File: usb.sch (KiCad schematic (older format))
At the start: 10 parts, among them J1 USB_B_Micro, Q1 2N2219, Q2 2N2219, U2 CP2102N-A01-GQFN28, U6 USBLC6-2SC6

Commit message: Reorganize symbols & update vendors
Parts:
- Q2: renamed from Q1; value 2N2219 -> ?
- Q3: renamed from Q2; value 2N2219 -> ?
- R4: renamed from R1; value 22.1 Ohm -> 22k Ohm; Vendor (none) -> avt.pl; VendorLink (none) -> https://sklep.avt.pl/avt701-805.html
- R5: renamed from R2; value 47.5 Ohm -> 47k Ohm; Vendor (none) -> avt.pl; VendorLink (none) -> https://sklep.avt.pl/avt701-805.html
- R6: renamed from R4; value 2k Ohm -> 2.2k Ohm; Vendor (none) -> avt.pl; VendorLink (none) -> https://sklep.avt.pl/avt701-805.html
- R7: renamed from R6; Vendor (none) -> avt.pl; VendorLink (none) -> https://sklep.avt.pl/avt701-805.html
- R8: renamed from R7; Vendor (none) -> avt.pl; VendorLink (none) -> https://sklep.avt.pl/avt701-805.html
- renumbered J1 to J6, U6 to U5, U2 to U6
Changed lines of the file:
@@
 P 5350 3700
 AR Path="/5FFBA0ED" Ref="U?"  Part="1"
-AR Path="/5FF73D59/5FFBA0ED" Ref="U2"  Part="1"
-F 0 "U2" H 5350 2300 50  0000 C CNN
-F 1 "CP2102N-A01-GQFN28" H 5350 2200 50  0000 C CNN
+AR Path="/5FF73D59/5FFBA0ED" Ref="U6"  Part="1"
+F 0 "U6" H 4900 4950 50  0000 C CNN
+F 1 "CP2102N-A01-GQFN28" H 5900 2350 50  0000 C CNN
 F 2 "Package_DFN_QFN:QFN-28-1EP_5x5mm_P0.5mm_EP3.35x3.35mm" H 5800 2500 50  0001 L CNN
 F 3 "https://www.silabs.com/documents/public/data-sheets/cp2102n-datasheet.pdf" H 5400 2950 50  0001 C CNN
@@
 P 5350 5350
 AR Path="/5FFBA0F3" Ref="#PWR?"  Part="1"
-AR Path="/5FF73D59/5FFBA0F3" Ref="#PWR05"  Part="1"
-F 0 "#PWR05" H 5350 5100 50  0001 C CNN
+AR Path="/5FF73D59/5FFBA0F3" Ref="#PWR027"  Part="1"
+F 0 "#PWR027" H 5350 5100 50  0001 C CNN
 F 1 "GND" H 5400 5150 50  0000 C CNN
 F 2 "" H 5350 5350 50  0001 C CNN
@@
 P 4750 2550
 AR Path="/5FFBA107" Ref="R?"  Part="1"
-AR Path="/5FF73D59/5FFBA107" Ref="R4"  Part="1"
-F 0 "R4" H 4900 2500 50  0000 R CNN
-F 1 "2k Ohm" H 5100 2600 50  0000 R CNN
+AR Path="/5FF73D59/5FFBA107" Ref="R6"  Part="1"
+F 0 "R6" H 4900 2500 50  0000 R CNN
+F 1 "2.2k Ohm" H 5100 2600 50  0000 R CNN
 F 2 "Resistor_SMD:R_0805_2012Metric_Pad1.20x1.40mm_HandSolder" V 4680 2550 50  0001 C CNN
 F 3 "~" H 4750 2550 50  0001 C CNN
+F 4 "avt.pl" H 4750 2550 50  0001 C CNN "Vendor"
+F 5 "https://sklep.avt.pl/avt701-805.html" H 4750 2550 50  0001 C CNN "VendorLink"
 	1    4750 2550
 	-1   0    0    1
@@
 P 4150 3300
 AR Path="/5FFBA115" Ref="R?"  Part="1"
-AR Path="/5FF73D59/5FFBA115" Ref="R2"  Part="1"
-F 0 "R2" H 4350 3250 50  0000 R CNN
-F 1 "47.5 Ohm" H 4600 3350 50  0000 R CNN
+AR Path="/5FF73D59/5FFBA115" Ref="R5"  Part="1"
+F 0 "R5" H 4350 3250 50  0000 R CNN
+F 1 "47k Ohm" H 4600 3350 50  0000 R CNN
 F 2 "Resistor_SMD:R_0805_2012Metric_Pad1.20x1.40mm_HandSolder" V 4080 3300 50  0001 C CNN
 F 3 "~" H 4150 3300 50  0001 C CNN
+F 4 "avt.pl" H 4150 3300 50  0001 C CNN "Vendor"
+F 5 "https://sklep.avt.pl/avt701-805.html" H 4150 3300 50  0001 C CNN "VendorLink"
 	1    4150 3300
 	-1   0    0    1
@@
 P 4150 2750
 AR Path="/5FFBA123" Ref="R?"  Part="1"
-AR Path="/5FF73D59/5FFBA123" Ref="R1"  Part="1"
-F 0 "R1" H 4300 2700 50  0000 R CNN
-F 1 "22.1 Ohm" H 4600 2800 50  0000 R CNN
+AR Path="/5FF73D59/5FFBA123" Ref="R4"  Part="1"
+F 0 "R4" H 4300 2700 50  0000 R CNN
+F 1 "22k Ohm" H 4600 2800 50  0000 R CNN
 F 2 "Resistor_SMD:R_0805_2012Metric_Pad1.20x1.40mm_HandSolder" V 4080 2750 50  0001 C CNN
 F 3 "~" H 4150 2750 50  0001 C CNN
+F 4 "avt.pl" H 4150 2750 50  0001 C CNN "Vendor"
+F 5 "https://sklep.avt.pl/avt701-805.html" H 4150 2750 50  0001 C CNN "VendorLink"
 	1    4150 2750
 	-1   0    0    1
@@
 P 4150 3650
 AR Path="/5FFBA14D" Ref="#PWR?"  Part="1"
-AR Path="/5FF73D59/5FFBA14D" Ref="#PWR03"  Part="1"
-F 0 "#PWR03" H 4150 3400 50  0001 C CNN
+AR Path="/5FF73D59/5FFBA14D" Ref="#PWR026"  Part="1"
+F 0 "#PWR026" H 4150 3400 50  0001 C CNN
 F 1 "GND" H 4200 3450 50  0000 C CNN
 F 2 "" H 4150 3650 50  0001 C CNN
@@
 P 1550 2650
 AR Path="/5FFC9948" Ref="J?"  Part="1"
-AR Path="/5FF73D59/5FFC9948" Ref="J1"  Part="1"
-F 0 "J1" H 1650 3150 50  0000 C CNN
+AR Path="/5FF73D59/5FFC9948" Ref="J6"  Part="1"
+F 0 "J6" H 1650 3150 50  0000 C CNN
 F 1 "USB_B_Micro" H 1650 3050 50  0000 C CNN
 F 2 "Connector_USB:USB_Micro-B_Molex_47346-0001" H 1700 2600 50  0001 C CNN
@@
 P 8600 2700
 AR Path="/5FFD7260" Ref="Q?"  Part="1"
-AR Path="/5FF73D59/5FFD7260" Ref="Q1"  Part="1"
-F 0 "Q1" H 8800 2750 50  0000 L CNN
-F 1 "2N2219" H 8800 2700 50  0000 L CNN
+AR Path="/5FF73D59/5FFD7260" Ref="Q2"  Part="1"
+F 0 "Q2" H 8800 2750 50  0000 L CNN
+F 1 "?" H 8800 2700 50  0000 L CNN
 F 2 "Package_TO_SOT_SMD:SOT-23" H 8800 2625 50  0001 L CIN
 F 3 "https://www.onsemi.com/pub/Collateral/BC808-D.pdf" H 8600 2700 50  0001 L CNN
@@
 P 8600 3250
 AR Path="/5FFD7266" Ref="Q?"  Part="1"
-AR Path="/5FF73D59/5FFD7266" Ref="Q2"  Part="1"
-F 0 "Q2" H 8850 3300 50  0000 L CNN
-F 1 "2N2219" H 8850 3250 50  0000 L CNN
+AR Path="/5FF73D59/5FFD7266" Ref="Q3"  Part="1"
+F 0 "Q3" H 8850 3300 50  0000 L CNN
+F 1 "?" H 8850 3250 50  0000 L CNN
 F 2 "Package_TO_SOT_SMD:SOT-23" H 8800 3175 50  0001 L CIN
 F 3 "https://www.onsemi.com/pub/Collateral/BC808-D.pdf" H 8600 3250 50  0001 L CNN
@@
 P 8100 2700
 AR Path="/5FFD726C" Ref="R?"  Part="1"
-AR Path="/5FF73D59/5FFD726C" Ref="R6"  Part="1"
-F 0 "R6" V 7850 2700 50  0000 C CNN
+AR Path="/5FF73D59/5FFD726C" Ref="R7"  Part="1"
+F 0 "R7" V 7850 2700 50  0000 C CNN
 F 1 "10k Ohm" V 7950 2700 50  0000 C CNN
 F 2 "Resistor_SMD:R_0805_2012Metric_Pad1.20x1.40mm_HandSolder" V 8030 2700 50  0001 C CNN
 F 3 "~" H 8100 2700 50  0001 C CNN
+F 4 "avt.pl" H 8100 2700 50  0001 C CNN "Vendor"
+F 5 "https://sklep.avt.pl/avt701-805.html" H 8100 2700 50  0001 C CNN "VendorLink"
 	1    8100 2700
 	0    1    1    0
@@
 P 8100 3250
 AR Path="/5FFD7272" Ref="R?"  Part="1"
-AR Path="/5FF73D59/5FFD7272" Ref="R7"  Part="1"
-F 0 "R7" V 7850 3250 50  0000 C CNN
+AR Path="/5FF73D59/5FFD7272" Ref="R8"  Part="1"
+F 0 "R8" V 7850 3250 50  0000 C CNN
 F 1 "10k Ohm" V 7950 3250 50  0000 C CNN
 F 2 "Resistor_SMD:R_0805_2012Metric_Pad1.20x1.40mm_HandSolder" V 8030 3250 50  0001 C CNN
 F 3 "~" H 8100 3250 50  0001 C CNN
+F 4 "avt.pl" H 8100 3250 50  0001 C CNN "Vendor"
+F 5 "https://sklep.avt.pl/avt701-805.html" H 8100 3250 50  0001 C CNN "VendorLink"
 	1    8100 3250
 	0    1    1    0
@@
 P 1800 4000
 AR Path="/5FFC9960" Ref="#PWR?"  Part="1"
-AR Path="/5FF73D59/5FFC9960" Ref="#PWR02"  Part="1"
-F 0 "#PWR02" H 1800 3750 50  0001 C CNN
+AR Path="/5FF73D59/5FFC9960" Ref="#PWR025"  Part="1"
+F 0 "#PWR025" H 1800 3750 50  0001 C CNN
 F 1 "GND" H 1850 3800 50  0000 C CNN
 F 2 "" H 1800 4000 50  0001 C CNN
@@
 Connection ~ 1800 3850
 $Comp
-L Power_Protection:USBLC6-2SC6 U6
+L Power_Protection:USBLC6-2SC6 U5
 U 1 1 601988F8
 P 2450 3200
-F 0 "U6" H 2450 3800 50  0000 C CNN
-F 1 "USBLC6-2SC6" H 2450 3700 50  0000 C CNN
+F 0 "U5" H 2700 3550 50  0000 C CNN
+F 1 "USBLC6-2SC6" H 2150 2800 50  0000 C CNN
 F 2 "Package_TO_SOT_SMD:SOT-23-6" H 2450 2700 50  0001 C CNN
 F 3 "https://www.st.com/resource/en/datasheet/usblc6-2.pdf" H 2650 3550 50  0001 C CNN

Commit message: Remove Op-Amp circuit for USB power
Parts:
- added D?: STPS0520Z, Diode_SMD:D_0805_2012Metric_Pad1.15x1.40mm_HandSolder, symbol Device:D_Schottky
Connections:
- net VBUS: now also D?.2 (A)
- new net +5V: D?.1 (K)
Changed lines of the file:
@@
 Wire Wire Line
 	4150 2200 3900 2200
-Text HLabel 3050 2450 2    50   Output ~ 0
-VBUS
 Text Label 2850 2450 2    50   ~ 0
 VBUS
@@
 Connection ~ 2450 2450
 Wire Wire Line
-	2450 2450 3050 2450
+	2450 2450 2850 2450
 Wire Wire Line
 	1550 3850 1800 3850
@@
 Wire Wire Line
 	5350 1850 5350 2300
+$Comp
+L Device:D_Schottky D?
+U 1 1 5FB2216A
+P 3000 5850
+AR Path="/5FB2216A" Ref="D?"  Part="1"
+AR Path="/5FF6344B/5FB2216A" Ref="D?"  Part="1"
+F 0 "D?" H 3000 5600 50  0000 C CNN
+F 1 "STPS0520Z" H 3000 5700 50  0000 C CNN
+F 2 "Diode_SMD:D_0805_2012Metric_Pad1.15x1.40mm_HandSolder" H 3000 5850 50  0001 C CNN
+F 3 "https://www.st.com/resource/en/datasheet/stps0520z.pdf" H 3000 5850 50  0001 C CNN
+F 4 "tme.eu" H 3000 5850 50  0001 C CNN "Vendor"
+F 5 "https://www.tme.eu/pl/details/stps0520z/diody-schottky-smd/stmicroelectronics/" H 3000 5850 50  0001 C CNN "VendorLink"
+	1    3000 5850
+	-1   0    0    1
+$EndComp
+Wire Wire Line
+	3150 5850 3650 5850
+Wire Wire Line
+	2200 5850 2850 5850
+Text HLabel 3650 5850 2    50   UnSpc ~ 0
++5V
+Text Label 2200 5850 0    50   ~ 0
+VBUS
 $EndSCHEMATC

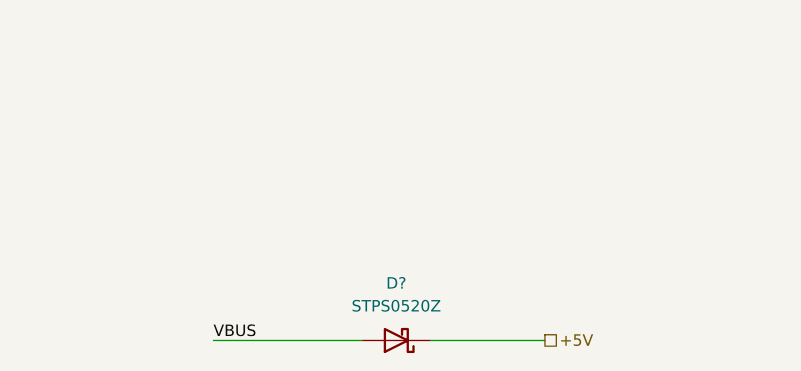
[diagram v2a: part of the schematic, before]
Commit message: Change footprint of D3
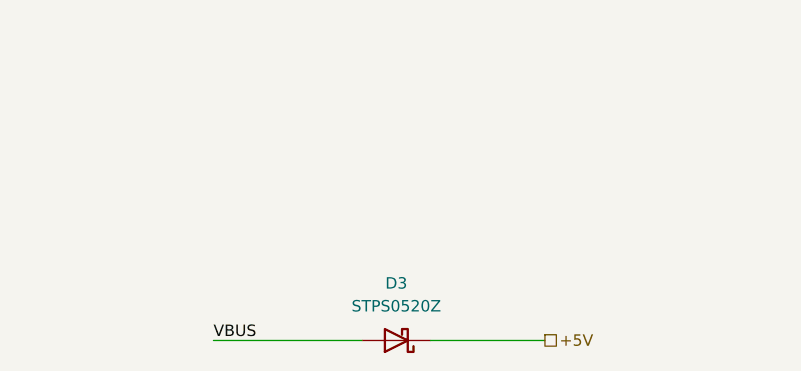
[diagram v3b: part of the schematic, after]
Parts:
- D3: renamed from D?; footprint Diode_SMD:D_0805_2012Metric_Pad1.15x1.40mm_HandSolder -> Diode_SMD:D_SOD-123
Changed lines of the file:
@@
 AR Path="/5FB2216A" Ref="D?"  Part="1"
 AR Path="/5FF6344B/5FB2216A" Ref="D?"  Part="1"
-F 0 "D?" H 3000 5600 50  0000 C CNN
+AR Path="/5FF73D59/5FB2216A" Ref="D3"  Part="1"
+F 0 "D3" H 3000 5600 50  0000 C CNN
 F 1 "STPS0520Z" H 3000 5700 50  0000 C CNN
-F 2 "Diode_SMD:D_0805_2012Metric_Pad1.15x1.40mm_HandSolder" H 3000 5850 50  0001 C CNN
+F 2 "Diode_SMD:D_SOD-123" H 3000 5850 50  0001 C CNN
 F 3 "https://www.st.com/resource/en/datasheet/stps0520z.pdf" H 3000 5850 50  0001 C CNN
 F 4 "tme.eu" H 3000 5850 50  0001 C CNN "Vendor"

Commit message: Update vendor for USB-UART and USBLC6
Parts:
- U5: Vendor (none) -> tme.eu; VendorLink (none) -> https://www.tme.eu/pl/details/usblc6-2sc6/diody-zabezpiecza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
- U6: Vendor (none) -> tme.eu; VendorLink (none) -> https://www.tme.eu/pl/details/cp2102-gm/uklady-scalone-inte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
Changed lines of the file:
@@
 F 2 "Package_DFN_QFN:QFN-28-1EP_5x5mm_P0.5mm_EP3.35x3.35mm" H 5800 2500 50  0001 L CNN
 F 3 "https://www.silabs.com/documents/public/data-sheets/cp2102n-datasheet.pdf" H 5400 2950 50  0001 C CNN
+F 4 "tme.eu" H 5350 3700 50  0001 C CNN "Vendor"
+F 5 "https://www.tme.eu/pl/details/cp2102-gm/uklady-scalone-interfejs-usb/silicon-labs/cp2102-gmr/" H 5350 3700 50  0001 C CNN "VendorLink"
 	1    5350 3700
 	1    0    0    -1
@@
 F 2 "Package_TO_SOT_SMD:SOT-23-6" H 2450 2700 50  0001 C CNN
 F 3 "https://www.st.com/resource/en/datasheet/usblc6-2.pdf" H 2650 3550 50  0001 C CNN
+F 4 "tme.eu" H 2450 3200 50  0001 C CNN "Vendor"
+F 5 "https://www.tme.eu/pl/details/usblc6-2sc6/diody-zabezpieczajace-drabinki/stmicroelectronics/" H 2450 3200 50  0001 C CNN "VendorLink"
 	1    2450 3200
 	-1   0    0    -1

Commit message: Fix auto-reset circuit for ESP32
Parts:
- Q2, Q3: symbol Transistor_BJT:BC807 -> Transistor_BJT:BC817
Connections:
- net DTR: now also Q3.2 (E); no longer Q3.3 (C)
- net IO0: now also Q3.3 (C); no longer Q3.2 (E)
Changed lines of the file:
@@
 RTS
 $Comp
-L Transistor_BJT:BC807 Q?
+L Transistor_BJT:BC817 Q?
 U 1 1 5FFD7260
 P 8600 2700
@@
 $EndComp
 $Comp
-L Transistor_BJT:BC807 Q?
+L Transistor_BJT:BC817 Q?
 U 1 1 5FFD7266
 P 8600 3250
@@
 F 3 "https://www.onsemi.com/pub/Collateral/BC808-D.pdf" H 8600 3250 50  0001 L CNN
 	1    8600 3250
-	1    0    0    -1
+	1    0    0    1
 $EndComp
 $Comp

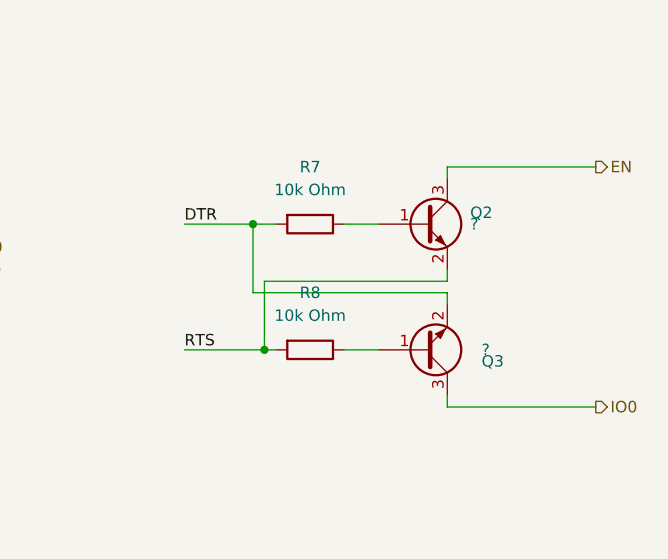
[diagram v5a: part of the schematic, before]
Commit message: Replace auto-reset circuit with single BCR129S chip
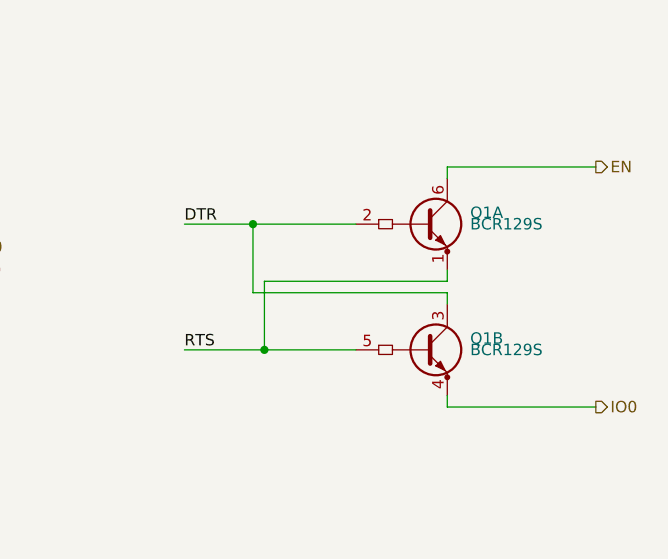
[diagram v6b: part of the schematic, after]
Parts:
- removed Q2, Q3: ?, Package_TO_SOT_SMD:SOT-23, symbol Transistor_BJT:BC817
- removed R7, R8: 10k Ohm, Resistor_SMD:R_0805_2012Metric_Pad1.20x1.40mm_HandSolder, symbol Device:R
- added Q1: BCR129S, Package_TO_SOT_SMD:SOT-363_SC-70-6, symbol Transistor_BJT:BCR129S
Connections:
- net DTR: now also Q1.2 (B1), Q1.3 (C1)
- net EN: now also Q1.6 (C1)
- net IO0: now also Q1.4 (E2)
- net RTS: now also Q1.1 (E1), Q1.5 (B2)
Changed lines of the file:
@@
 Text Label 7550 3250 0    50   ~ 0
 RTS
-$Comp
-L Transistor_BJT:BC817 Q?
-U 1 1 5FFD7260
-P 8600 2700
-AR Path="/5FFD7260" Ref="Q?"  Part="1"
-AR Path="/5FF73D59/5FFD7260" Ref="Q2"  Part="1"
-F 0 "Q2" H 8800 2750 50  0000 L CNN
-F 1 "?" H 8800 2700 50  0000 L CNN
-F 2 "Package_TO_SOT_SMD:SOT-23" H 8800 2625 50  0001 L CIN
-F 3 "https://www.onsemi.com/pub/Collateral/BC808-D.pdf" H 8600 2700 50  0001 L CNN
-	1    8600 2700
-	1    0    0    -1
-$EndComp
-$Comp
-L Transistor_BJT:BC817 Q?
-U 1 1 5FFD7266
-P 8600 3250
-AR Path="/5FFD7266" Ref="Q?"  Part="1"
-AR Path="/5FF73D59/5FFD7266" Ref="Q3"  Part="1"
-F 0 "Q3" H 8850 3300 50  0000 L CNN
-F 1 "?" H 8850 3250 50  0000 L CNN
-F 2 "Package_TO_SOT_SMD:SOT-23" H 8800 3175 50  0001 L CIN
-F 3 "https://www.onsemi.com/pub/Collateral/BC808-D.pdf" H 8600 3250 50  0001 L CNN
-	1    8600 3250
-	1    0    0    1
-$EndComp
-$Comp
-L Device:R R?
-U 1 1 5FFD726C
-P 8100 2700
-AR Path="/5FFD726C" Ref="R?"  Part="1"
-AR Path="/5FF73D59/5FFD726C" Ref="R7"  Part="1"
-F 0 "R7" V 7850 2700 50  0000 C CNN
-F 1 "10k Ohm" V 7950 2700 50  0000 C CNN
-F 2 "Resistor_SMD:R_0805_2012Metric_Pad1.20x1.40mm_HandSolder" V 8030 2700 50  0001 C CNN
-F 3 "~" H 8100 2700 50  0001 C CNN
-F 4 "avt.pl" H 8100 2700 50  0001 C CNN "Vendor"
-F 5 "https://sklep.avt.pl/avt701-805.html" H 8100 2700 50  0001 C CNN "VendorLink"
-	1    8100 2700
-	0    1    1    0
-$EndComp
-$Comp
-L Device:R R?
-U 1 1 5FFD7272
-P 8100 3250
-AR Path="/5FFD7272" Ref="R?"  Part="1"
-AR Path="/5FF73D59/5FFD7272" Ref="R8"  Part="1"
-F 0 "R8" V 7850 3250 50  0000 C CNN
-F 1 "10k Ohm" V 7950 3250 50  0000 C CNN
-F 2 "Resistor_SMD:R_0805_2012Metric_Pad1.20x1.40mm_HandSolder" V 8030 3250 50  0001 C CNN
-F 3 "~" H 8100 3250 50  0001 C CNN
-F 4 "avt.pl" H 8100 3250 50  0001 C CNN "Vendor"
-F 5 "https://sklep.avt.pl/avt701-805.html" H 8100 3250 50  0001 C CNN "VendorLink"
-	1    8100 3250
-	0    1    1    0
-$EndComp
 Wire Wire Line
 	7550 2700 7850 2700
 Wire Wire Line
-	8250 2700 8400 2700
-Wire Wire Line
 	7550 3250 7900 3250
-Wire Wire Line
-	8250 3250 8400 3250
 Wire Wire Line
 	7900 3250 7900 2950
@@
 Connection ~ 7900 3250
 Wire Wire Line
-	7900 3250 7950 3250
+	7900 3250 8300 3250
 Wire Wire Line
 	8700 2900 8700 2950
@@
 Connection ~ 7850 2700
 Wire Wire Line
-	7850 2700 7950 2700
+	7850 2700 8300 2700
 Wire Wire Line
 	8700 3450 8700 3500
@@
 Text Label 2200 5850 0    50   ~ 0
 VBUS
+$Comp
+L Transistor_BJT:BCR129S Q1
+U 1 1 5FB53DE1
+P 8650 2700
+F 0 "Q1" H 8800 2750 50  0000 L CNN
+F 1 "BCR129S" H 8800 2700 50  0000 L CNN
+F 2 "Package_TO_SOT_SMD:SOT-363_SC-70-6" H 8655 2260 50  0001 C CNN
+F 3 "https://www.infineon.com/dgdl/Infineon-BCR129SERIES-DS-v01_01-en.pdf?fileId=db3a30431428a37301143f7ab7820287" H 8650 2700 50  0001 C CNN
+F 4 "tme.eu" H 8650 2700 50  0001 C CNN "Vendor"
+F 5 "https://www.tme.eu/pl/details/bcr129sh6327/tranzystory-npn-smd/infineon-technologies/" H 8650 2700 50  0001 C CNN "VendorLink"
+	1    8650 2700
+	1    0    0    -1
+$EndComp
+$Comp
+L Transistor_BJT:BCR129S Q1
+U 2 1 5FB59A80
+P 8650 3250
+F 0 "Q1" H 8800 3300 50  0000 L CNN
+F 1 "BCR129S" H 8800 3250 50  0000 L CNN
+F 2 "Package_TO_SOT_SMD:SOT-363_SC-70-6" H 8655 2810 50  0001 C CNN
+F 3 "https://www.infineon.com/dgdl/Infineon-BCR129SERIES-DS-v01_01-en.pdf?fileId=db3a30431428a37301143f7ab7820287" H 8650 3250 50  0001 C CNN
+F 4 "tme.eu" H 8650 3250 50  0001 C CNN "Vendor"
+F 5 "https://www.tme.eu/pl/details/bcr129sh6327/tranzystory-npn-smd/infineon-technologies/" H 8650 3250 50  0001 C CNN "VendorLink"
+	2    8650 3250
+	1    0    0    -1
+$EndComp
 $EndSCHEMATC

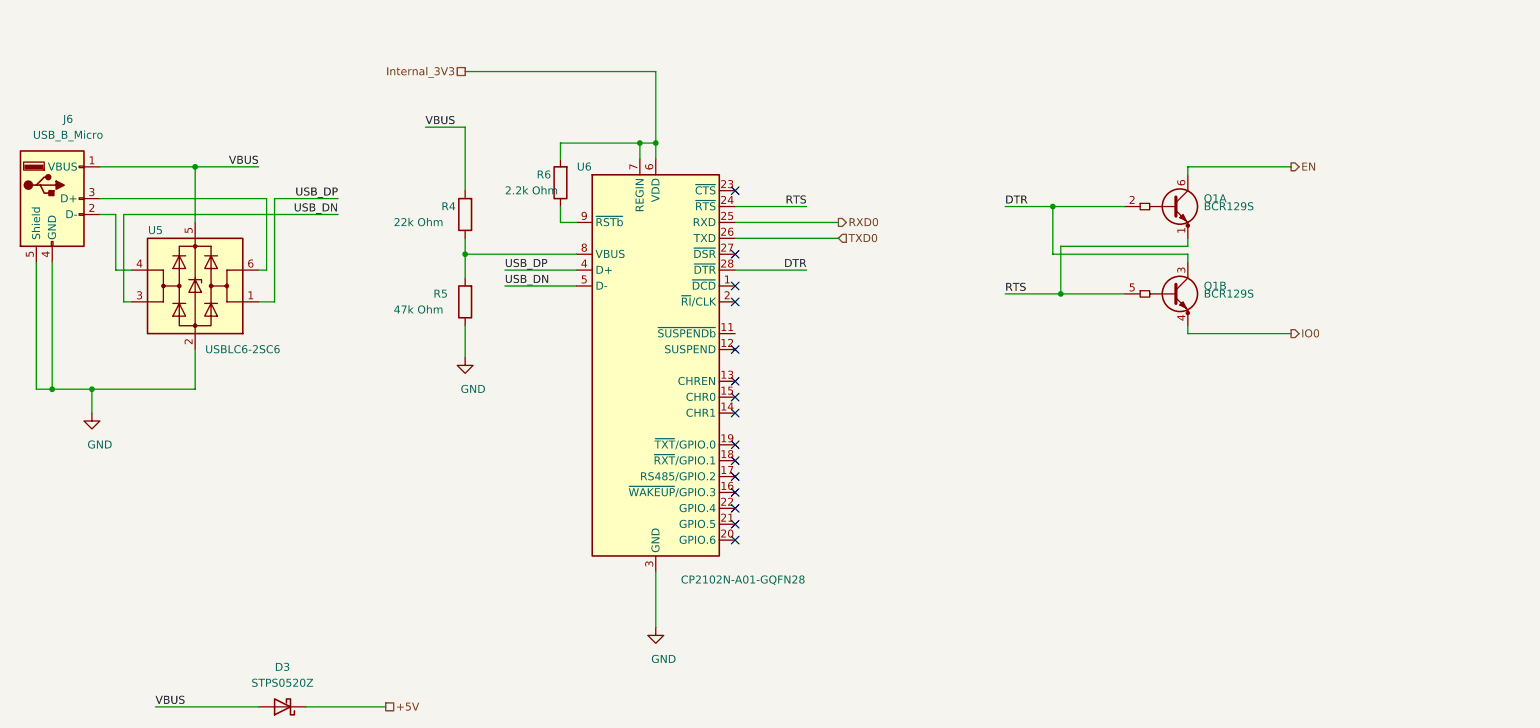
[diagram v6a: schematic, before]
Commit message: Schematic reorganization & reannotate
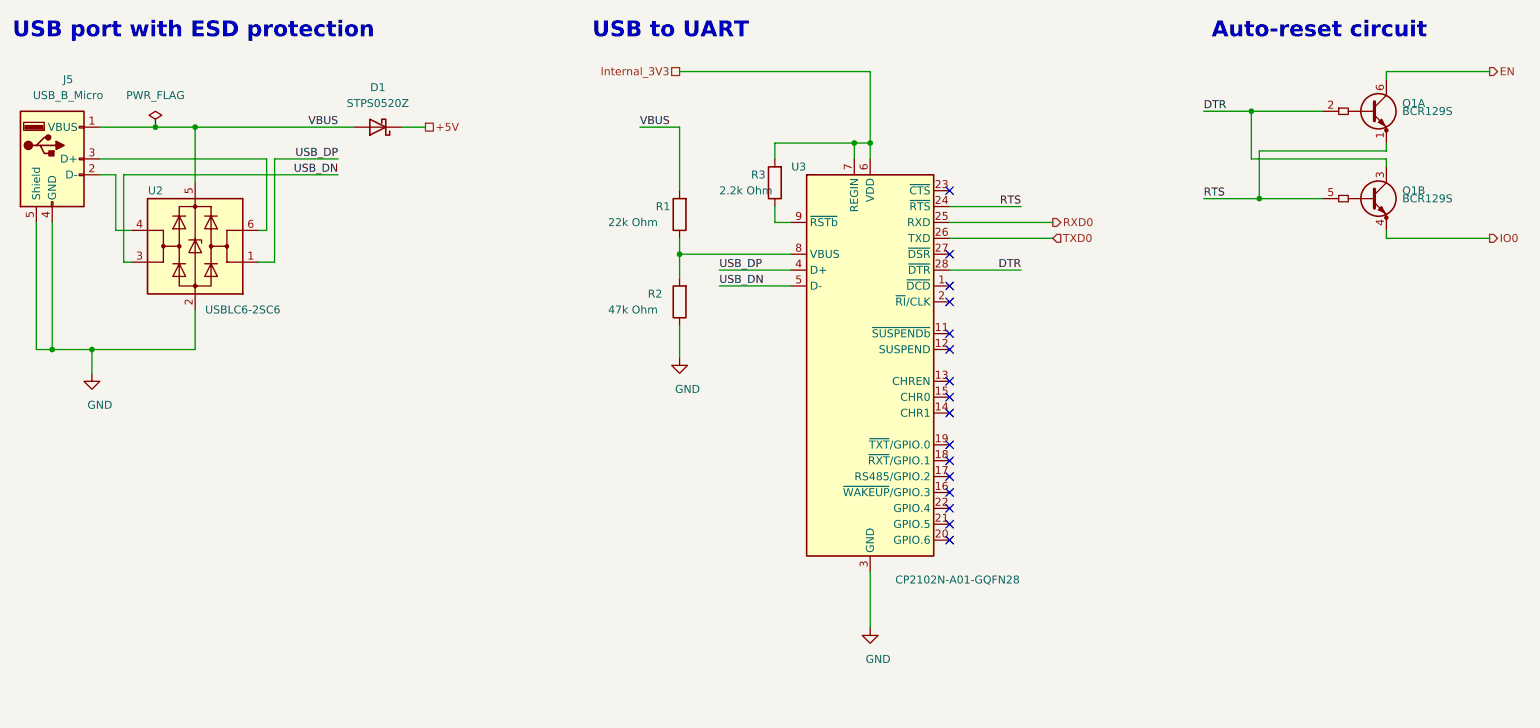
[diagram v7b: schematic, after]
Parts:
- renumbered D3 to D1, J6 to J5, R4 to R1, R5 to R2, R6 to R3, U5 to U2, U6 to U3
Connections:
- no-connect marks 15 -> 16
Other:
- note added: "Auto-reset circuit"
- note added: "USB port with ESD protection"
- note added: "USB to UART"
- moved on the sheet: D1, J5, Q1A, Q1B, R1, R2, R3, U2, U3
